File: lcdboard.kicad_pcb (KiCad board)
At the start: 2 copper layers, 64 x 120.5 mm, 68 parts, among them J1 Conn_02x05_Odd_Even, J2 Conn_02x25_Counter_Clockwise, J3 Conn_02x12_Counter_Clockwise, J4 USB_B_Micro, J5 Conn_01x03, SW1 SW_Push, SW3 SW_SPST, U1 MK82FN256VLL15, U2 Serial-Flash, U3 TPS61169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

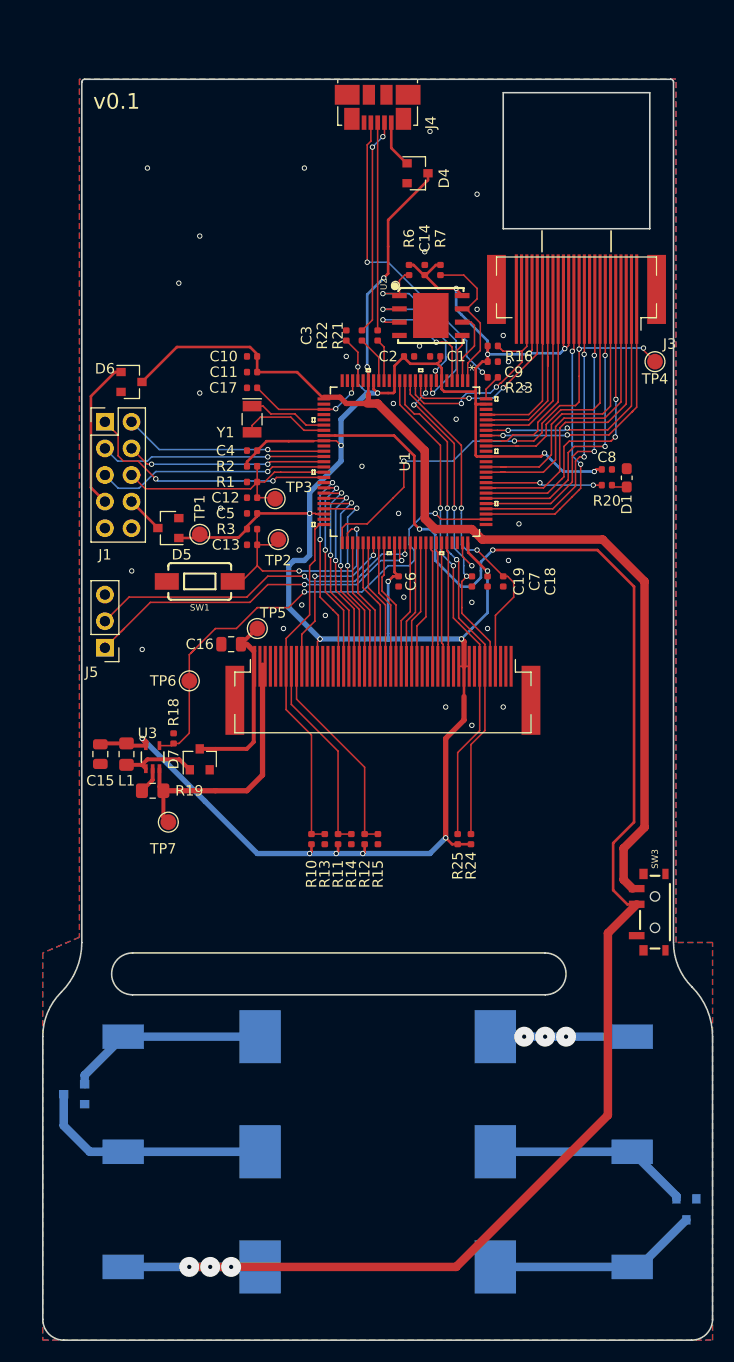
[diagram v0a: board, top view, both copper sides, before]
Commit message: Connect backlight supply to VREGIN
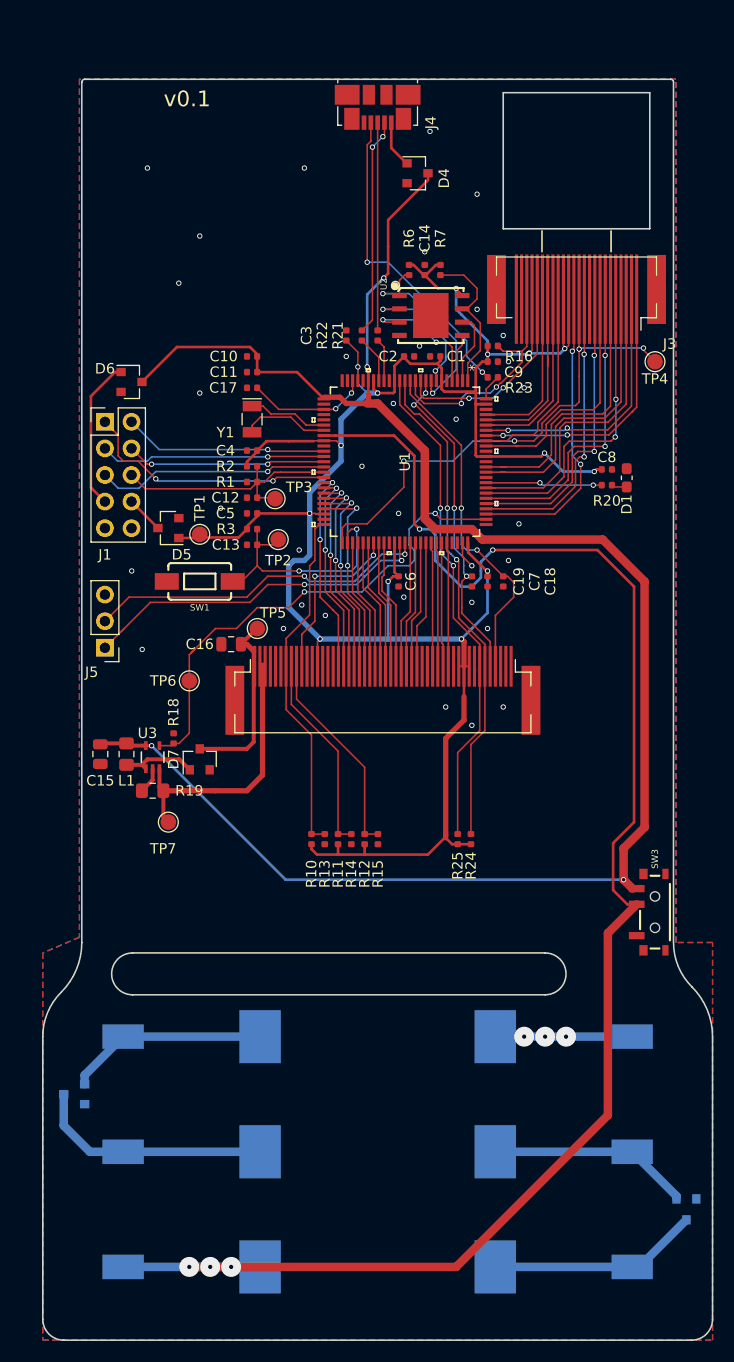
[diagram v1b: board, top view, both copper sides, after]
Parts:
- R20: value 180 -> 91
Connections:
- C15 pad 1: +3V3 -> /VDD_REGIN
- L1 pad 1: +3V3 -> /VDD_REGIN
- U3 pad 5: +3V3 -> /VDD_REGIN
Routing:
- net /VDD_REGIN: track 119.2 -> 174.6 mm, vias 2 -> 4
- net +3V3: track 250.6 -> 224.6 mm, vias 19 -> 14
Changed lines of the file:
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@@
     (thickness 1.6)
     (drawings 23)
-    (tracks 1000)
+    (tracks 999)
     (zones 0)
     (modules 68)
@@
     )
     (pad 1 smd roundrect (at -0.9375 0 270) (size 0.975 1.4) (layers F.Cu F.Paste F.Mask) (roundrect_rratio 0.25)
-      (net 3 +3V3))
+      (net 10 /VDD_REGIN))
     (pad 2 smd roundrect (at 0.9375 0 270) (size 0.975 1.4) (layers F.Cu F.Paste F.Mask) (roundrect_rratio 0.25)
       (net 2 GND))
@@
     )
     (pad 1 smd roundrect (at -1.025 0 270) (size 1.15 1.4) (layers F.Cu F.Paste F.Mask) (roundrect_rratio 0.217391)
-      (net 3 +3V3))
+      (net 10 /VDD_REGIN))
     (pad 2 smd roundrect (at 1.025 0 270) (size 1.15 1.4) (layers F.Cu F.Paste F.Mask) (roundrect_rratio 0.217391)
       (net 87 "Net-(D7-Pad2)"))
@@
       (effects (font (size 1 1) (thickness 0.15)))
     )
-    (fp_text value 180 (at 0 1.17) (layer F.Fab) hide
+    (fp_text value 91 (at 0 1.17) (layer F.Fab) hide
       (effects (font (size 1 1) (thickness 0.15)))
     )
@@
       (net 73 /BKLT_PWM))
     (pad 5 smd rect (at 0 -2.2) (size 0.35 0.85) (layers F.Cu F.Paste F.Mask)
-      (net 3 +3V3))
+      (net 10 /VDD_REGIN))
   )
-  (gr_text v0.1 (at -24.9428 -40.3606) (layer F.SilkS)
+  (gr_text v0.1 (at -18.2 -40.6) (layer F.SilkS)
     (effects (font (size 1.5 1.5) (thickness 0.3)))
   )
@@
   (via (at -5 8.75) (size 0.508) (drill 0.3302) (layers F.Cu B.Cu) (net 2))
   (via (at 9 19.25) (size 0.508) (drill 0.3302) (layers F.Cu B.Cu) (net 2))
-  (segment (start -1.245142 31.325142) (end -1.42 31.5) (width 0.254) (layer F.Cu) (net 3))
-  (via (at -1.42 31.5) (size 0.508) (drill 0.3302) (layers F.Cu B.Cu) (net 3))
-  (segment (start -1.245142 30.610623) (end -1.245142 31.325142) (width 0.254) (layer F.Cu) (net 3))
-  (segment (start -3.785142 31.325142) (end -3.96 31.5) (width 0.254) (layer F.Cu) (net 3))
-  (via (at -3.96 31.5) (size 0.508) (drill 0.3302) (layers F.Cu B.Cu) (net 3))
-  (segment (start -3.785142 30.610623) (end -3.785142 31.325142) (width 0.254) (layer F.Cu) (net 3))
   (segment (start 9.409058 -11.439376) (end 9.560624 -11.439376) (width 0.254) (layer F.Cu) (net 3))
   (segment (start 9.366257 -11.482177) (end 9.409058 -11.439376) (width 0.254) (layer F.Cu) (net 3))
@@
   (segment (start 2.515 -15.902572) (end 2.515 -16) (width 0.254) (layer F.Cu) (net 3))
   (segment (start 3.118582 -15.29899) (end 2.515 -15.902572) (width 0.254) (layer F.Cu) (net 3))
-  (segment (start -23.784377 21.190623) (end -24 20.975) (width 0.381) (layer F.Cu) (net 3))
-  (segment (start -22.150142 21.190623) (end -23.784377 21.190623) (width 0.381) (layer F.Cu) (net 3))
-  (segment (start -26.4125 20.975) (end -26.5 21.0625) (width 0.381) (layer F.Cu) (net 3))
-  (segment (start -24 20.975) (end -26.4125 20.975) (width 0.381) (layer F.Cu) (net 3))
   (segment (start 8.75 13.61) (end 7.75 13.61) (width 0.1524) (layer F.Cu) (net 3))
   (segment (start 8.25 16.5) (end 8.25 16.75) (width 0.254) (layer F.Cu) (net 3))
@@
   (segment (start 7.110623 30.610623) (end 8.914858 30.610623) (width 0.254) (layer F.Cu) (net 3))
   (segment (start 6.5 30) (end 7.110623 30.610623) (width 0.254) (layer F.Cu) (net 3))
-  (via (at -6.5 31.5) (size 0.508) (drill 0.3302) (layers F.Cu B.Cu) (net 3))
-  (segment (start -6.325142 30.610623) (end -6.325142 31.325142) (width 0.254) (layer F.Cu) (net 3))
-  (segment (start -6.325142 31.325142) (end -6.5 31.5) (width 0.254) (layer F.Cu) (net 3))
-  (segment (start -6.5 31.5) (end -1.42 31.5) (width 0.508) (layer B.Cu) (net 3))
-  (segment (start -1.42 31.5) (end 5 31.5) (width 0.508) (layer B.Cu) (net 3))
-  (via (at 6.5 30) (size 0.508) (drill 0.3302) (layers F.Cu B.Cu) (net 3))
-  (segment (start 5 31.5) (end 6.5 30) (width 0.508) (layer B.Cu) (net 3))
-  (via (at -22.5 20.5) (size 0.508) (drill 0.3302) (layers F.Cu B.Cu) (net 3))
-  (segment (start -22.150142 20.849858) (end -22.5 20.5) (width 0.508) (layer F.Cu) (net 3))
-  (segment (start -22.150142 21.190623) (end -22.150142 20.849858) (width 0.508) (layer F.Cu) (net 3))
   (via (at 0 -12.5) (size 0.508) (drill 0.3302) (layers F.Cu B.Cu) (net 3))
   (via (at 8 11) (size 0.508) (drill 0.3302) (layers F.Cu B.Cu) (net 3))
@@
   (segment (start -11.515 -0.735) (end -11.515 -1) (width 0.254) (layer F.Cu) (net 3))
   (segment (start -12.485 0.235) (end -11.515 -0.735) (width 0.254) (layer F.Cu) (net 3))
-  (segment (start -11.5 31.5) (end -6.5 31.5) (width 0.508) (layer B.Cu) (net 3))
-  (segment (start -22.5 20.5) (end -16.5 26.5) (width 0.508) (layer B.Cu) (net 3))
-  (segment (start -16.5 26.5) (end -11.5 31.5) (width 0.508) (layer B.Cu) (net 3))
   (segment (start 8.25 18.75) (end 8.25 16.5) (width 0.508) (layer F.Cu) (net 3))
-  (segment (start 6.5 30) (end 6.5 20.5) (width 0.508) (layer F.Cu) (net 3))
   (segment (start 6.5 20.5) (end 8.25 18.75) (width 0.508) (layer F.Cu) (net 3))
+  (segment (start 6.5 29.7) (end 6.5 20.5) (width 0.508) (layer F.Cu) (net 3))
+  (segment (start 6.5 30) (end 6.5 29.7) (width 0.508) (layer F.Cu) (net 3))
+  (segment (start -5.8 31.6) (end -6.325142 31.074858) (width 0.254) (layer F.Cu) (net 3))
+  (segment (start -6.325142 31.074858) (end -6.325142 30.610623) (width 0.254) (layer F.Cu) (net 3))
+  (segment (start 6.5 29.7) (end 6.5 29.9) (width 0.254) (layer F.Cu) (net 3))
+  (segment (start 6.5 29.9) (end 4.8 31.6) (width 0.254) (layer F.Cu) (net 3))
+  (segment (start -3.785142 31.585142) (end -3.8 31.6) (width 0.254) (layer F.Cu) (net 3))
+  (segment (start -3.785142 30.610623) (end -3.785142 31.585142) (width 0.254) (layer F.Cu) (net 3))
+  (segment (start -3.8 31.6) (end -5.8 31.6) (width 0.254) (layer F.Cu) (net 3))
+  (segment (start -1.245142 31.554858) (end -1.2 31.6) (width 0.254) (layer F.Cu) (net 3))
+  (segment (start -1.245142 30.610623) (end -1.245142 31.554858) (width 0.254) (layer F.Cu) (net 3))
+  (segment (start 4.8 31.6) (end -1.2 31.6) (width 0.254) (layer F.Cu) (net 3))
+  (segment (start -1.2 31.6) (end -3.8 31.6) (width 0.254) (layer F.Cu) (net 3))
   (via (at -14 71) (size 1.905) (drill 0.4) (layers F.Cu B.Cu) (net 4))
   (via (at -16 71) (size 1.905) (drill 0.4) (layers F.Cu B.Cu) (net 4))
@@
   (segment (start 1.3 -35.91) (end 2.76 -34.45) (width 0.254) (layer F.Cu) (net 9) (status 20))
   (segment (start 1.3 -38.34) (end 1.3 -35.91) (width 0.254) (layer F.Cu) (net 9) (status 10))
+  (segment (start -23.784377 21.190623) (end -24 20.975) (width 0.381) (layer F.Cu) (net 10))
+  (segment (start -22.150142 21.190623) (end -23.784377 21.190623) (width 0.381) (layer F.Cu) (net 10))
+  (segment (start -26.4125 20.975) (end -26.5 21.0625) (width 0.381) (layer F.Cu) (net 10))
+  (segment (start -24 20.975) (end -26.4125 20.975) (width 0.381) (layer F.Cu) (net 10))
   (segment (start 4.81 -32.846) (end 1 -29.036) (width 0.254) (layer F.Cu) (net 10))
   (segment (start 4.81 -33.5) (end 4.81 -32.846) (width 0.254) (layer F.Cu) (net 10) (status 10))
@@
   (segment (start -0.890143 -14.890143) (end -1 -15) (width 0.254) (layer F.Cu) (net 10))
   (segment (start -0.890143 -13.686377) (end -0.890143 -14.890143) (width 0.254) (layer F.Cu) (net 10))
+  (via (at 23.5 34) (size 0.508) (drill 0.3302) (layers F.Cu B.Cu) (net 10))
+  (via (at -21.6 21.2) (size 0.508) (drill 0.3302) (layers F.Cu B.Cu) (net 10))
+  (segment (start -22.150142 21.190623) (end -21.609377 21.190623) (width 0.254) (layer F.Cu) (net 10))
+  (segment (start -21.609377 21.190623) (end -21.6 21.2) (width 0.254) (layer F.Cu) (net 10))
+  (segment (start -8.8 34) (end 23.5 34) (width 0.254) (layer B.Cu) (net 10))
+  (segment (start -21.6 21.2) (end -8.8 34) (width 0.254) (layer B.Cu) (net 10))
   (segment (start -21 0.390765) (end -23.520142 -2.129377) (width 0.254) (layer F.Cu) (net 11) (status 30))
   (segment (start -21 0.4) (end -21 0.390765) (width 0.254) (layer F.Cu) (net 11) (status 30))

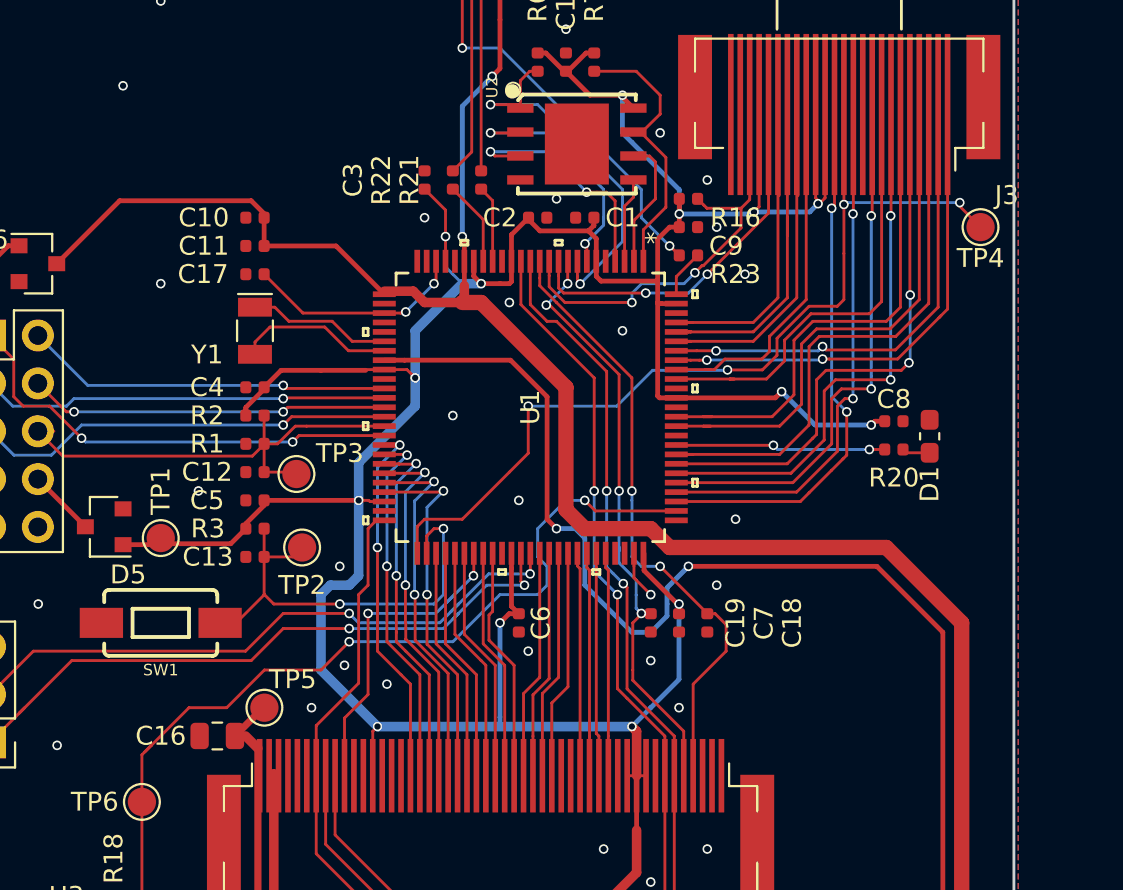
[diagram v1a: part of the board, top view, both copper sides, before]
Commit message: Add external oscillator
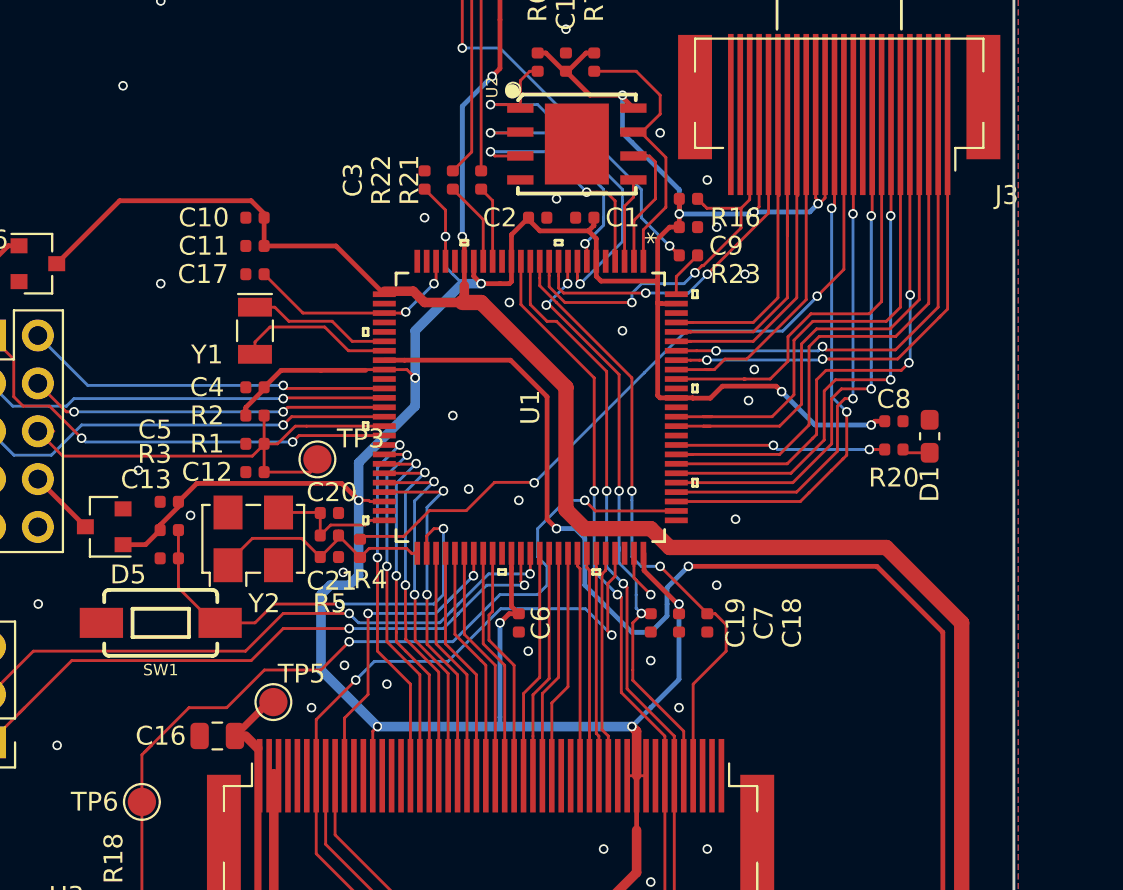
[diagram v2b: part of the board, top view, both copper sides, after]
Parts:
- removed TP1, TP2, TP4: TestPoint, TestPoint:TestPoint_Pad_D1.5mm
- added C20: 22pF, Capacitor_SMD:C_0402_1005Metric, F.Cu at (-8.05, -0.33)
- added C21: 22pF, Capacitor_SMD:C_0402_1005Metric, F.Cu at (-8.05, 2.01)
- added R4: 0, Resistor_SMD:R_0402_1005Metric, F.Cu at (-6.43, 1.55)
- added R5: 1M, Resistor_SMD:R_0402_1005Metric, F.Cu at (-8.05, 0.86)
- added Y2: 12MHz, Oscillator:Oscillator_SMD_EuroQuartz_XO53-4Pin_5.0x3.2mm_HandSoldering, F.Cu at (-12.1, 1.04)
- moved C13 4.55 mm to (-16.5, 2.08)
- moved C5 4.55 mm to (-16.5, -0.92)
- moved R3 4.55 mm to (-16.5, 0.58)
- moved TP3 1.36 mm to (-8.69, -3.17)
- moved TP5 0.56 mm to (-11.0, 9.70)
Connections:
- U1 pad 50: /DISP_IM0 -> /EXTAL0
- U1 pad 51: /CAM_XCLK1 -> /XTAL0_12MHZ
- U1 pad 72: Net-(U1-Pad72) -> /DISP_IM0
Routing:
- net /XTAL0_12MHZ: track 0.00 -> 13.4 mm
- net /DISP_IM0: track 34.1 -> 44.6 mm, vias 0 -> 2
- net /CAM_XCLK1: track 48.8 -> 39.6 mm, vias 4 -> 2
- net /EXTAL0: track 0.00 -> 8.04 mm
- net /NMI_b: track 25.2 -> 26.7 mm
- net /RST_b: track 24.1 -> 24.8 mm
- net +3V3: track 224.6 -> 225.4 mm
- net GND: vias 37 -> 41
